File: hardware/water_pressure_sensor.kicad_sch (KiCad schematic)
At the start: 6 parts

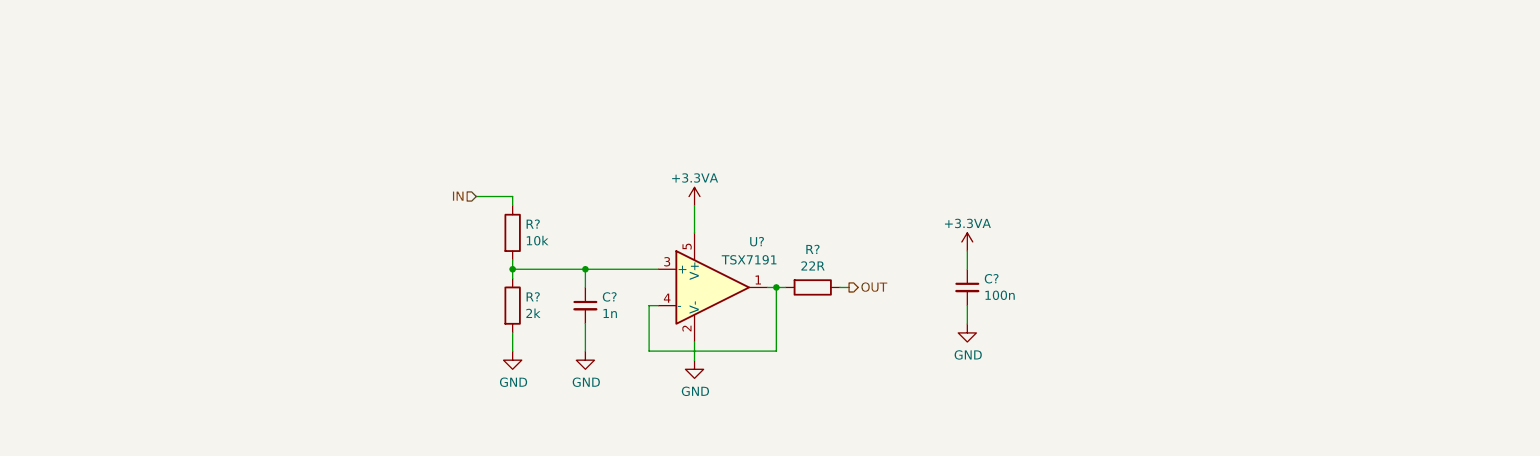
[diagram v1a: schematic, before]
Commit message: Improve the schematic
- add anti-aliasing filters
- rearrange the main connector signals
- improve the power filtering
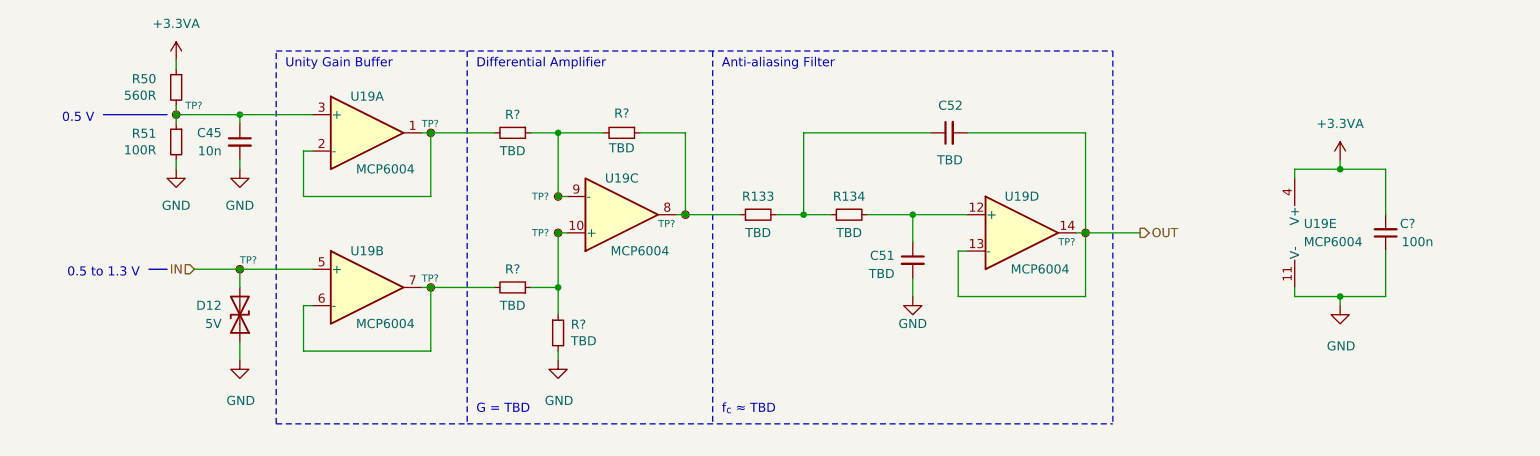
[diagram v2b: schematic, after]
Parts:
- removed C?: 100n, Capacitor_SMD:C_0603_1608Metric, symbol Device:C_Small
- removed C?: 1n, Capacitor_SMD:C_0603_1608Metric, symbol Device:C_Small
- removed R?: 10k, Resistor_SMD:R_0603_1608Metric, symbol Device:R
- removed R?: 2k, Resistor_SMD:R_0603_1608Metric, symbol Device:R
- removed R?: 22R, Resistor_SMD:R_0603_1608Metric, symbol Device:R
- removed U?: TSX7191, Package_TO_SOT_SMD:SOT-23-5, symbol Amplifier_Operational:OPA340NA
- added C45: 10n, symbol Device:C_Small
- added C51, C52: TBD, Capacitor_SMD:C_0603_1608Metric_Pad1.08x0.95mm_HandSolder, symbol Device:C_Small
- added C?: 100n, Capacitor_SMD:C_0603_1608Metric, symbol Device:C_Small
- added D12: 5V, symbol Device:D_TVS
- added R133, R134: TBD, Resistor_SMD:R_0603_1608Metric_Pad0.98x0.95mm_HandSolder, symbol Device:R_Small
- added R50: 560R, Resistor_SMD:R_0603_1608Metric_Pad0.98x0.95mm_HandSolder, symbol Device:R_Small
- added R51: 100R, Resistor_SMD:R_0603_1608Metric_Pad0.98x0.95mm_HandSolder, symbol Device:R_Small
- added R? (x4): TBD, Resistor_SMD:R_0603_1608Metric, symbol Device:R_Small
- added TP? (x8): TestPoint_Small, TestPoint:TestPoint_Pad_D1.0mm, symbol Connector:TestPoint_Small
- added U19: MCP6004, symbol Amplifier_Operational:MCP6004
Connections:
- net +3.3VA: now also C?.2, R50.1, U19.4 (V+)
- net GND: now also C45.2, C51.2, C?.1, D12.1 (A1), R51.2, R?.2, U19.11 (V-)
- net IN: now also D12.2 (A2), TP?.1, U19.5 (+)
- net OUT: now also C52.2, TP?.1, U19.13 (-), U19.14
- new net: C45.1, R50.2, R51.1, TP?.1, U19.3 (+)
- new net: R?.1, R?.1, TP?.1, U19.10 (+)
- new net: R?.2, TP?.1, U19.6 (-), U19.7
- new net: R?.1, R?.2, TP?.1, U19.9 (-)
- new net: R?.2, TP?.1, U19.1, U19.2 (-)
- new net: R133.1, R?.1, TP?.1, U19.8
- new net: C52.1, R133.2, R134.1
- new net: C51.1, R134.2, U19.12 (+)
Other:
- note added: "0.5 V"
- note added: "0.5 to 1.3 V"
- note added: "Anti-aliasing Filter"
- note added: "Differential Amplifier"
- note added: "G = TBD"
- note added: "Unity Gain Buffer"
- note added: "f_{c} ≈ TBD"

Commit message: Set component values
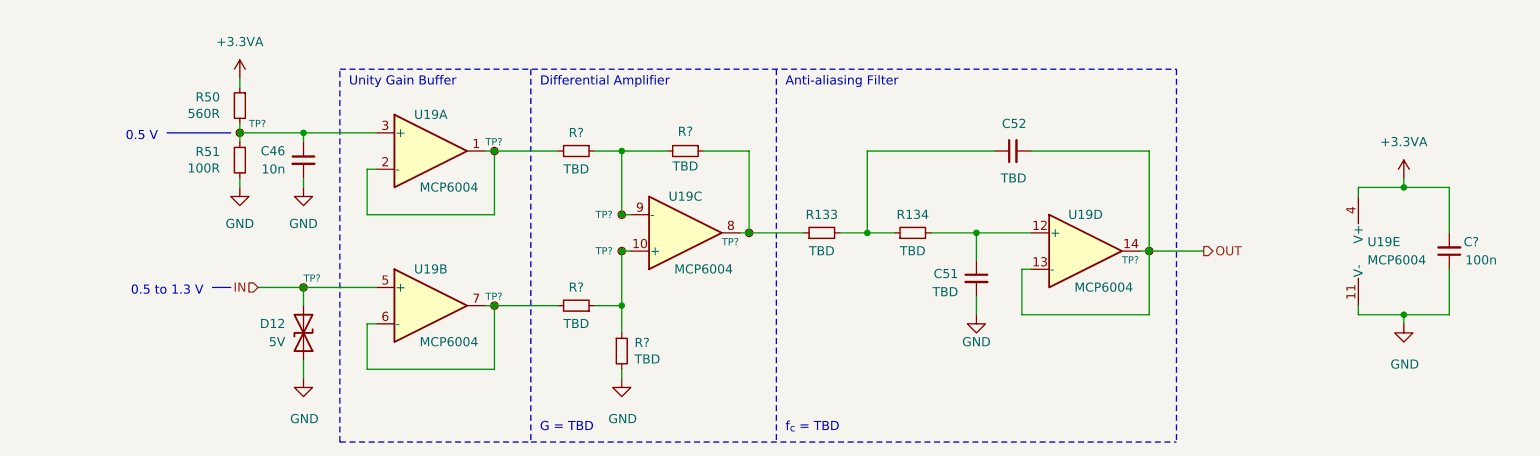
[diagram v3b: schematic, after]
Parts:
- C46: renamed from C45; footprint (none) -> Capacitor_SMD:C_0603_1608Metric
- C51, C52: footprint Capacitor_SMD:C_0603_1608Metric_Pad1.08x0.95mm_HandSolder -> Capacitor_SMD:C_0603_1608Metric
- R133, R134, R50, R51: footprint Resistor_SMD:R_0603_1608Metric_Pad0.98x0.95mm_HandSolder -> Resistor_SMD:R_0603_1608Metric
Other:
- note added: "f_{c} = TBD"
- note removed: "f_{c} ≈ TBD"
- moved on the sheet: C46, C51, C52, C?, D12, R133, R134, R50, R51, R?, TP?, U19A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

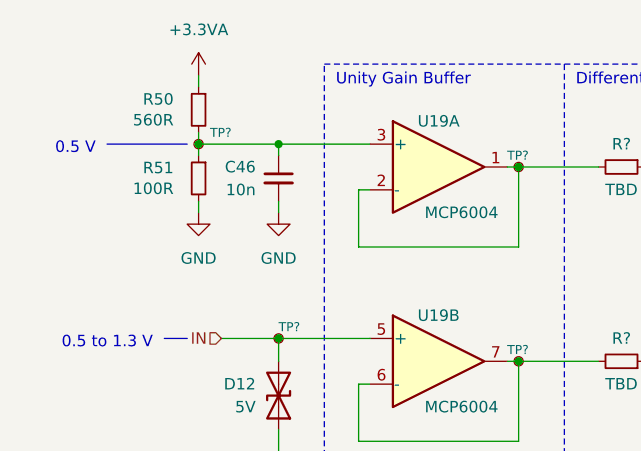
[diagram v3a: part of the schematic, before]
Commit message: Improve the schematic according to the feedback
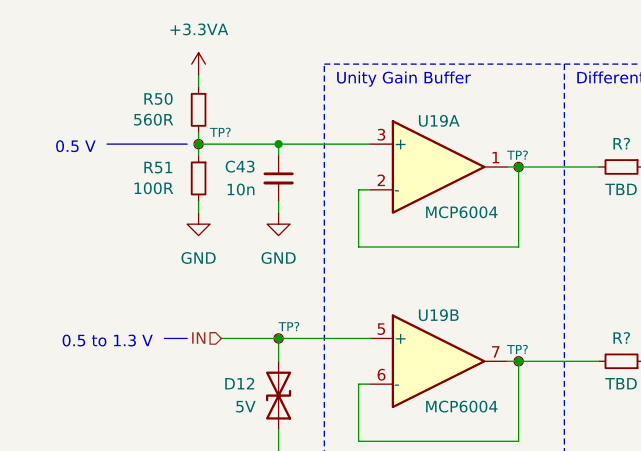
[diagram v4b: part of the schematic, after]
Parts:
- renumbered C46 to C43

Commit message: Use in-amps
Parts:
- removed C51, C52: TBD, Capacitor_SMD:C_0603_1608Metric, symbol Device:C_Small
- removed C?: 100n, Capacitor_SMD:C_0603_1608Metric, symbol Device:C_Small
- removed D12: 5V, symbol Device:D_TVS
- removed R133, R134, R? (x4): TBD, Resistor_SMD:R_0603_1608Metric, symbol Device:R_Small
- removed TP? (x7): TestPoint_Small, TestPoint:TestPoint_Pad_D1.0mm, symbol Connector:TestPoint_Small
- removed U19: MCP6004, symbol Amplifier_Operational:MCP6004
- added C? (x2): TBD, Capacitor_SMD:C_0603_1608Metric, symbol Device:C_Small
- added C? (x2): 100n, Capacitor_SMD:C_0603_1608Metric, symbol Device:C_Small
- added D14: 5V, symbol Device:D_TVS
- added R? (x4): TBD, Resistor_SMD:R_0603_1608Metric, symbol Device:R_Small
- added TP? (x4): TestPoint_Small, TestPoint:TestPoint_Pad_D1.0mm, symbol Connector:TestPoint_Small
- added U?: MCP6N11-005, Package_DFN_QFN:TDFN-8-1EP_3x2mm_P0.5mm_EP1.80x1.65mm, symbol MCP6N11:MCP6N11
- added U?: MCP6001, Package_TO_SOT_SMD:SOT-23-5, symbol Amplifier_Operational:MCP6001-OT
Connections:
- net +3.3VA: now also C?.1, C?.1, U?.5 (V+), U?.7 (V+), U?.8 (EN)
- net GND: now also C?.2, C?.2, C?.2, D14.1 (A1), R?.1, U?.2 (V-), U?.4 (V-), U?.5 (RF), U?.9 (EP)
- net IN: now also D14.2 (A2), TP?.1, U?.3 (+)
- net OUT: now also C?.2, TP?.1, U?.1, U?.4 (-)
- net at C43.1, R50.2, R51.1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: now also TP?.1, U?.2 (-)
- new net: C?.1, R?.1, R?.2
- new net: C?.1, R?.2, U?.3 (+)
- new net: R?.1, R?.2, U?.1 (FG)
- new net: R?.1, R?.2, TP?.1, U?.6
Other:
- note added: "Instrumentation Amplifier"
- note removed: "Differential Amplifier"
- note removed: "Unity Gain Buffer"
- moved on the sheet: C43, R50, R51, TP?

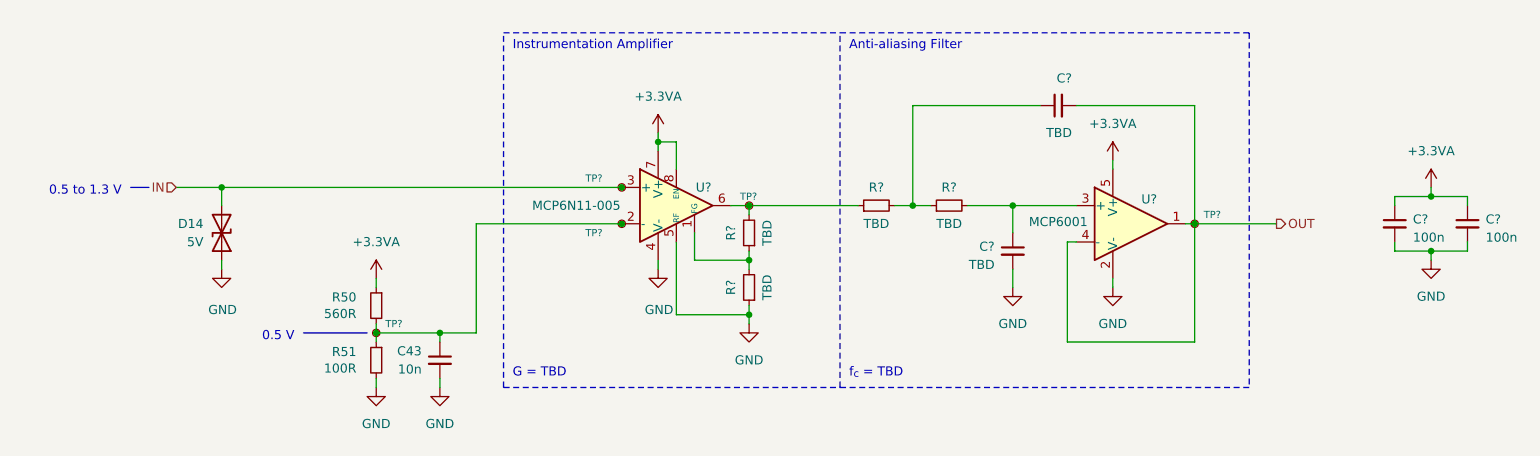
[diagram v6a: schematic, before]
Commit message: Improve the diagram based on the feedback
- add an input LC filter
- remove the USB connector
- add a programmer connector
- move optocouplers into a subsheet
- add a suspension tension meter IC
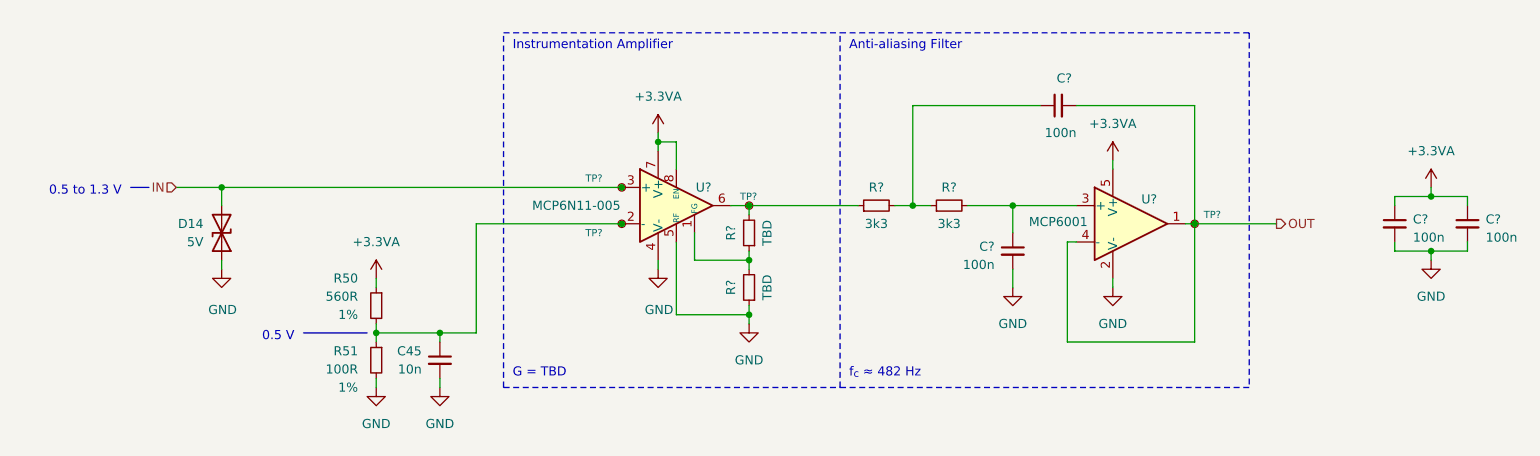
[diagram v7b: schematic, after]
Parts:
- removed TP?: TestPoint_Small, TestPoint:TestPoint_Pad_D1.0mm, symbol Connector:TestPoint_Small
- C? (x2): value TBD -> 100n
- D14: footprint (none) -> Diode_SMD:D_SOD-523; Component (none) -> PESD5V0V1BB-QX
- R50, R51: Tolerance (none) -> 1%
- R? (x2): value TBD -> 3k3
- renumbered C43 to C45
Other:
- note added: "f_{c} ≈ 482 Hz"
- note removed: "f_{c} = TBD"
